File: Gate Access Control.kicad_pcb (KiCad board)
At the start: 2 copper layers, 85.4 x 38 mm, 20 parts, among them J1 Screw_Terminal_01x02, J2 RF Receiver 433MHz, J3 Conn_01x08, J4 IR_SENSORT, J5 Screw_Terminal_01x04, J6 Screw_Terminal_01x02, J7 Screw_Terminal_01x02, J8 Conn_01x06, U1 ATmega328-MM, Y1 Crystal

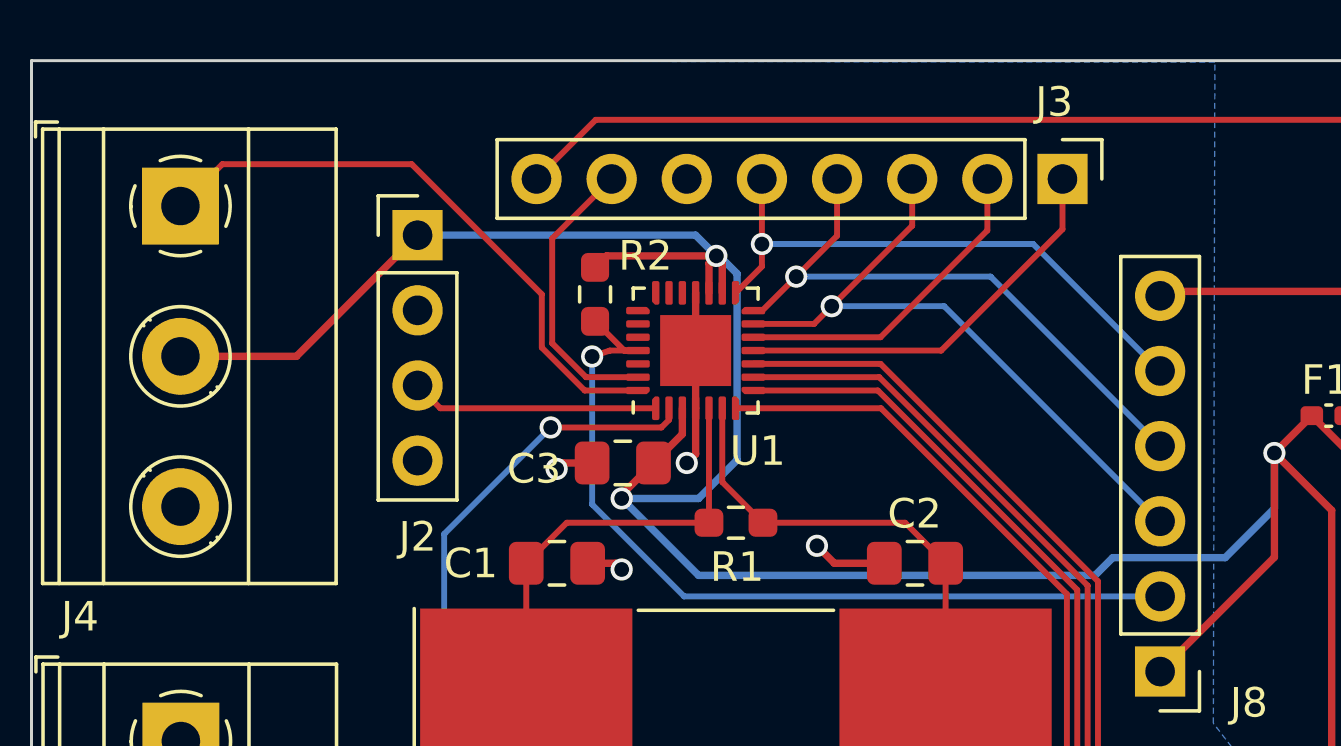
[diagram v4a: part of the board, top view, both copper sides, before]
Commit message: Changed Symbol and footprint of RF Receiver
RF Receiver dad one unnecessary unconnected pin.
Edited PCB design accordingly.
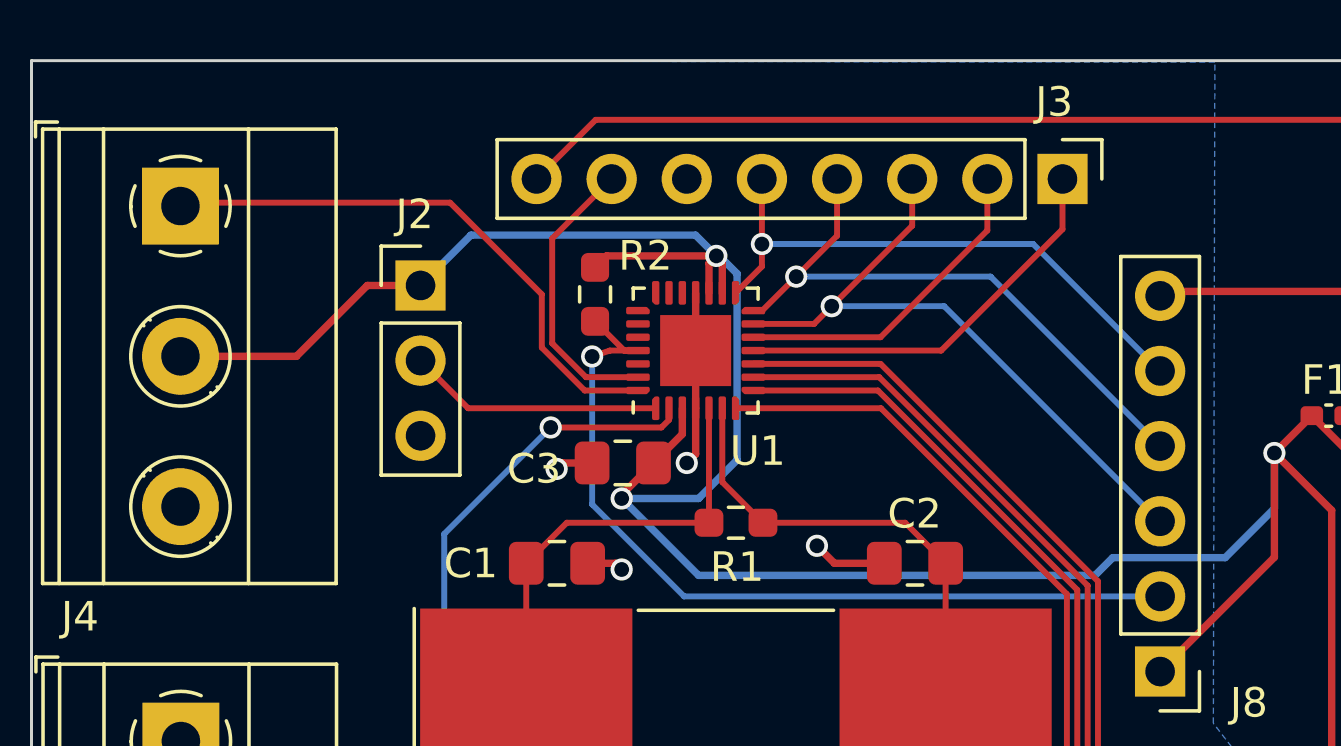
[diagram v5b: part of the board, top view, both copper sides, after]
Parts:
- J2: footprint Connector_PinHeader_2.54mm:PinHeader_1x04_P2.54mm_Vertical -> Connector_PinHeader_2.54mm:PinHeader_1x03_P2.54mm_Vertical
- moved J2 1.70 mm to (65.6, 62.6)
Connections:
- J2 pad 2: unconnected-(J2-DATA-Pad2) -> /RF receiver - PWM
- J2 pad 3: /RF receiver - PWM -> GND
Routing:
- net /IR Sensor - DI: track 20.3 -> 19.2 mm

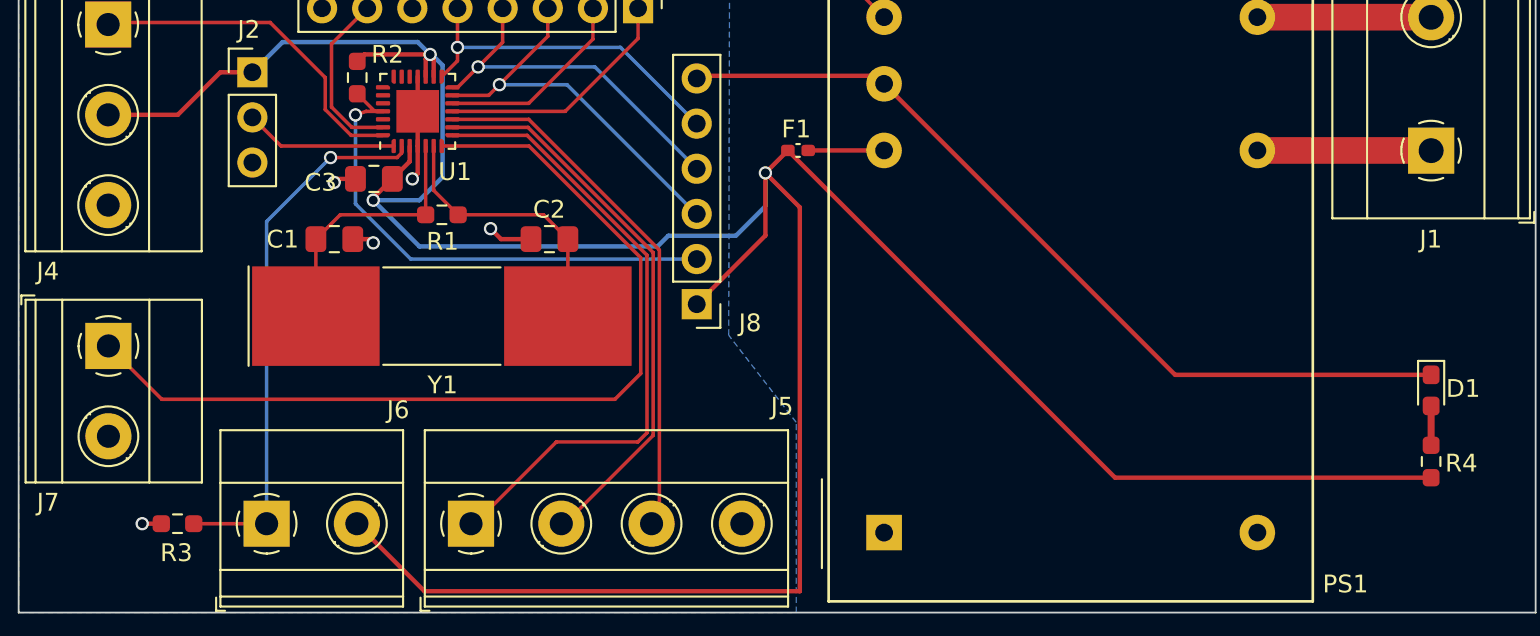
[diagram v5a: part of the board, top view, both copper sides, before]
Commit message: Assigned Smaller Footprint for Crystal
Also changed fuse value and footprint.
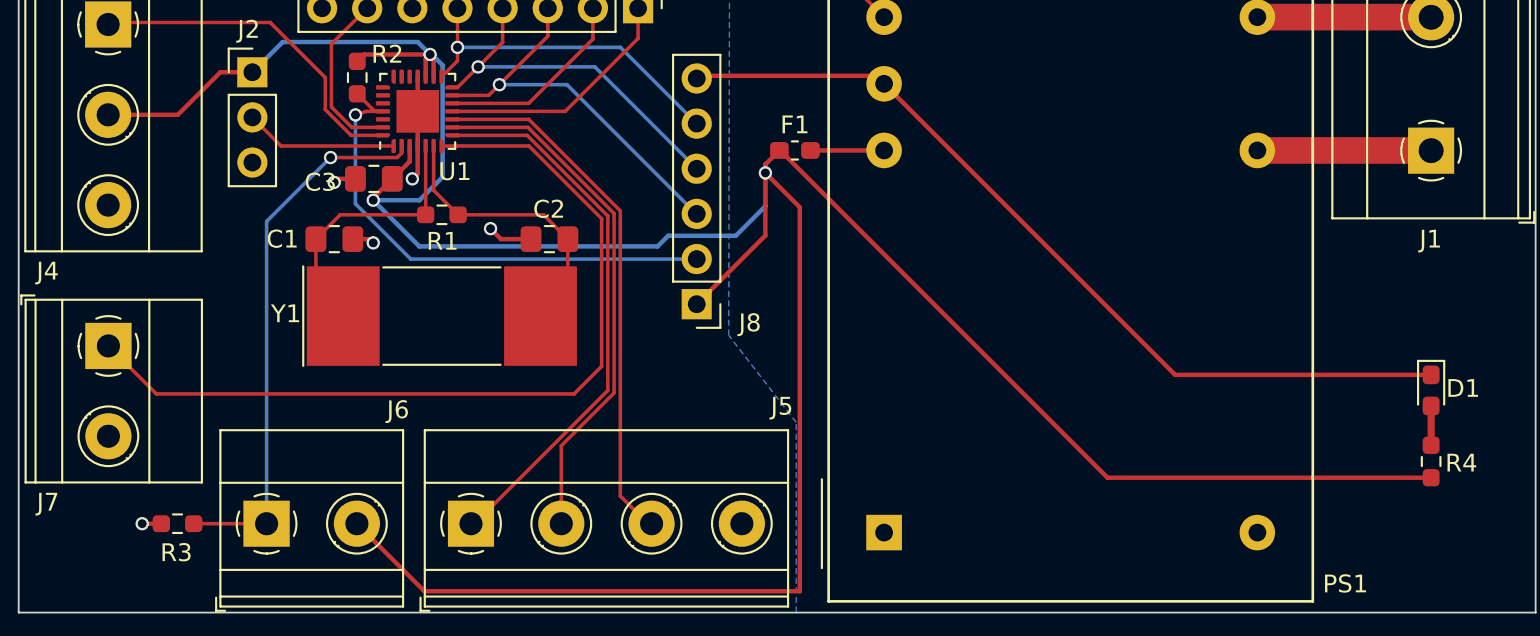
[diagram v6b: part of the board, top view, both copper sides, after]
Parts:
- F1: value 200 mA -> 500 mA; footprint Fuse:Fuse_0402_1005Metric_Pad0.77x0.64mm_HandSolder -> Fuse:Fuse_0603_1608Metric_Pad1.05x0.95mm_HandSolder
- Y1: footprint Crystal:Crystal_SMD_SeikoEpson_MA505-2Pin_12.7x5.1mm_HandSoldering -> Crystal:Crystal_SMD_SeikoEpson_MA505-2Pin_12.7x5.1mm
- moved F1 0.17 mm to (96.1, 67.0)
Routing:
- net /Inverter PWM: track 35.8 -> 31.3 mm
- net /Flashing Lights: track 52.1 -> 48.5 mm
- net /Enable: track 31.8 -> 30.0 mm
- net /XTAL1: track 14.9 -> 15.6 mm
- net /XTAL2: track 15.5 -> 16.2 mm

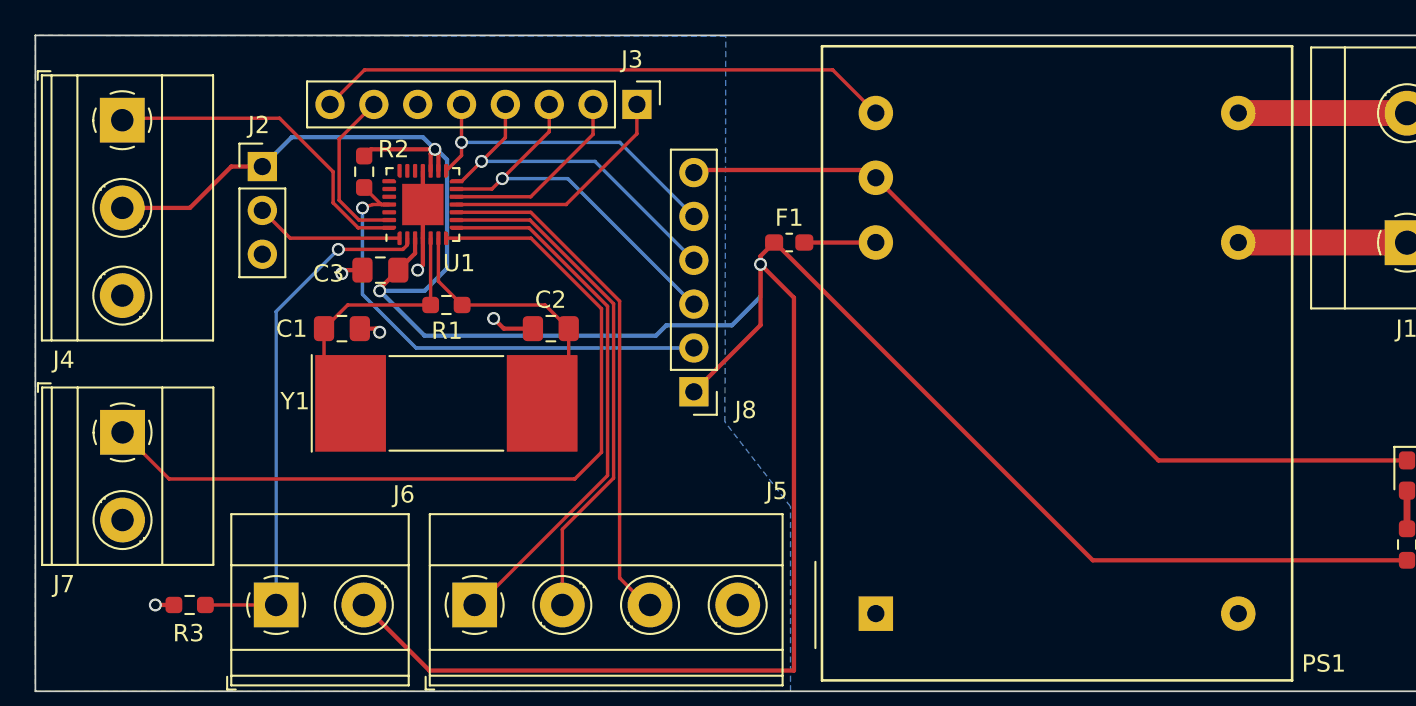
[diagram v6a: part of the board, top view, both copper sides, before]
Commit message: Even Smaller Crystal Footprint and added Labels for External Connections
Also Beautified Schematic Layout
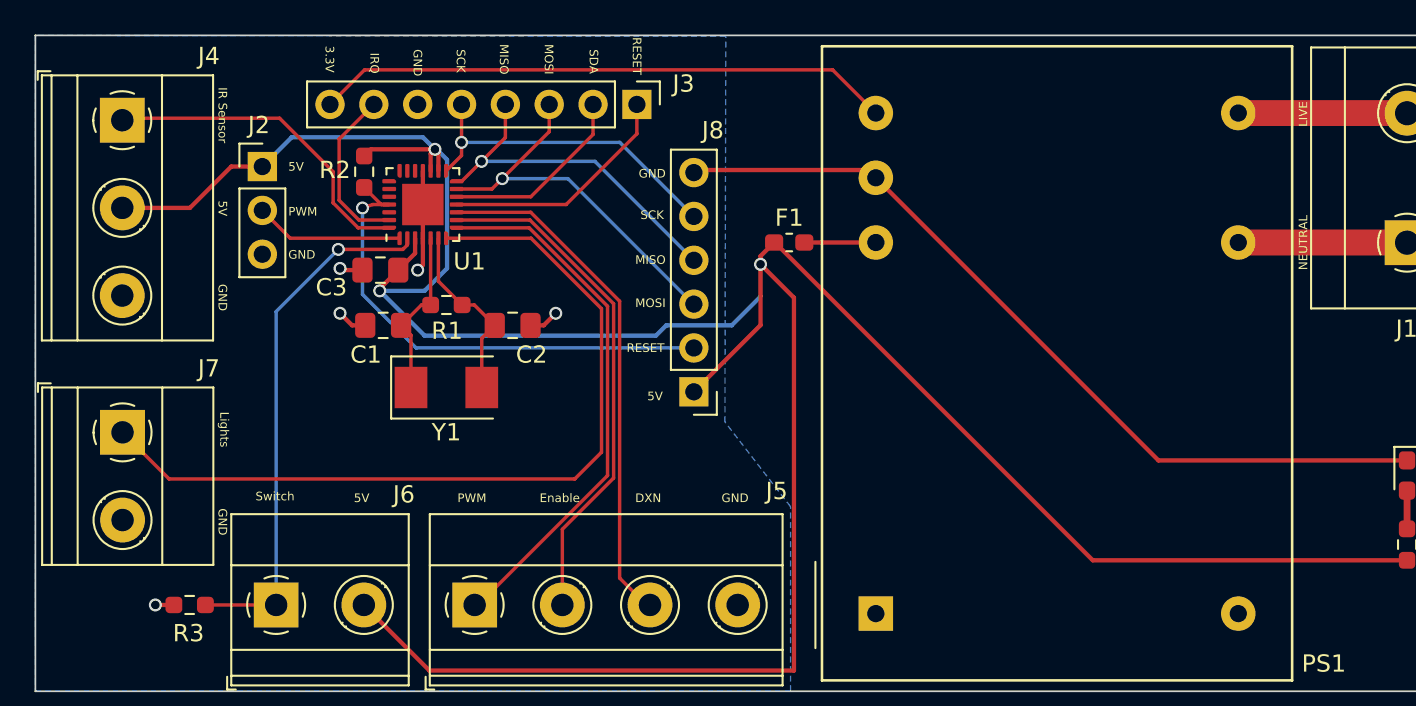
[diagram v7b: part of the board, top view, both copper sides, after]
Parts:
- Y1: footprint Crystal:Crystal_SMD_SeikoEpson_MA505-2Pin_12.7x5.1mm -> Crystal:Crystal_SMD_Abracon_ABM3-2Pin_5.0x3.2mm
- moved C1 2.40 mm to (72.6, 71.8), turned to 0 degrees
- moved C2 2.22 mm to (80.1, 71.8), turned to 180 degrees
- moved Y1 0.92 mm to (76.3, 75.4)
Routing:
- net /XTAL1: track 15.6 -> 9.91 mm
- net /XTAL2: track 16.2 -> 10.7 mm
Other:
- board text added: "3.3V"
- board text added: "5V"
- board text added: "DXN"
- board text added: "Enable"
- board text added: "GND"
- board text added: "IR Sensor"
- board text added: "IRQ"
- board text added: "LIVE"
- board text added: "Lights"
- board text added: "MISO"
- board text added: "MOSI"
- board text added: "NEUTRAL"
- board text added: "PWM"
- board text added: "RESET"
- board text added: "SCK"
- board text added: "SDA"
- board text added: "Switch"
